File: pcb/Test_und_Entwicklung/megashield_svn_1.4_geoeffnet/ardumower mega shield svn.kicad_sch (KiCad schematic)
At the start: 21 parts, among them K3 RELAY_2RT, P16 RPI Backup P., P17 RPI Main P., P42 Charger, P43 Battery, P49 MotorStop, Q1 BC847B

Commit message: megashield_svn_1.4_geoeffnet
megashield_svn_1.4_geoeffnet
29 BY1-BY12 JLCCPCB Nummer ergänzt
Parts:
- D10: Funktion Schalt-Diode, 75 V, 150 mA, SOD-123 -> (none); JLCPCB LCSC Part (none) -> C81598
- D77: JLCPCB LCSC Part (none) -> C81598
- EF1: JLCPCB Basic / Extern (none) -> 1; JLCPCB LCSC Part (none) -> C83797
- EF2: JLCPCB Basic / Extern (none) -> 1; JLCPCB LCSC Part (none) -> C312012
- EF3: JLCPCB Basic / Extern (none) -> 1; JLCPCB LCSC Part (none) -> C312004
- K3: Printfassung für Relais R: FIN 95.15.2 -> (none)
- Q1: JLCPCB Basic / Extern (none) -> 1; JLCPCB LCSC Part (none) -> C8575
- R10, R13: JLCPCB LCSC Part (none) -> C95519
- R12, R9: JLCPCB LCSC Part (none) -> C95527
- R18: JLCPCB LCSC Part (none) -> C4190
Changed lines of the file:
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@@
       (effects (font (size 1.27 1.27)) hide)
     )
-    (property "JLCPCB LCSC Part" "" (id 6) (at 111.76 62.484 0)
+    (property "JLCPCB LCSC Part" "C95527" (id 6) (at 111.76 62.484 0)
       (effects (font (size 1.27 1.27)) hide)
     )
@@
       (effects (font (size 1.27 1.27)) hide)
     )
-    (property "JLCPCB LCSC Part" "" (id 6) (at 111.76 78.232 0)
+    (property "JLCPCB LCSC Part" "C95519" (id 6) (at 111.76 78.232 0)
       (effects (font (size 1.27 1.27)) hide)
     )
@@
       (effects (font (size 1.27 1.27)) hide)
     )
-    (property "JLCPCB LCSC Part" "" (id 6) (at 133.858 99.568 0)
+    (property "JLCPCB LCSC Part" "C4190" (id 6) (at 133.858 99.568 0)
       (effects (font (size 1.27 1.27)) hide)
     )
@@
       (effects (font (size 1.27 1.27)) hide)
     )
-    (property "JLCPCB LCSC Part" "" (id 6) (at 212.725 69.469 0)
+    (property "JLCPCB LCSC Part" "C95527" (id 6) (at 212.725 69.469 0)
       (effects (font (size 1.27 1.27)) hide)
     )
@@
       (effects (font (size 1.27 1.27)) hide)
     )
-    (property "JLCPCB LCSC Part" "" (id 6) (at 212.725 85.217 0)
+    (property "JLCPCB LCSC Part" "C95519" (id 6) (at 212.725 85.217 0)
       (effects (font (size 1.27 1.27)) hide)
     )
@@
       (effects (font (size 1.27 1.27)) hide)
     )
+    (property "JLCPCB Basic / Extern" "1" (id 6) (at 52.197 51.816 0)
+      (effects (font (size 1.27 1.27)) hide)
+    )
+    (property "JLCPCB LCSC Part" "C83797" (id 7) (at 52.197 51.816 0)
+      (effects (font (size 1.27 1.27)) hide)
+    )
   )
   (symbol (lib_id "ardumower-mega-shield-svn-rescue:F_10A-RESCUE-ardumower_mega_shield_svn") (at 186.69 52.959 270) (unit 1)
@@
       (effects (font (size 1.27 1.27)) hide)
     )
+    (property "JLCPCB Basic / Extern" "1" (id 6) (at 186.69 52.959 0)
+      (effects (font (size 1.27 1.27)) hide)
+    )
+    (property "JLCPCB LCSC Part" "C312012" (id 7) (at 186.69 52.959 0)
+      (effects (font (size 1.27 1.27)) hide)
+    )
   )
   (symbol (lib_id "ardumower-mega-shield-svn-rescue:F_10A-RESCUE-ardumower_mega_shield_svn") (at 201.803 39.116 270) (unit 1)
@@
       (effects (font (size 1.27 1.27)) hide)
     )
+    (property "JLCPCB Basic / Extern" "1" (id 6) (at 201.803 39.116 0)
+      (effects (font (size 1.27 1.27)) hide)
+    )
+    (property "JLCPCB LCSC Part" "C312004" (id 7) (at 201.803 39.116 0)
+      (effects (font (size 1.27 1.27)) hide)
+    )
   )
   (symbol (lib_id "ardumower-mega-shield-svn-rescue:CP_Small-RESCUE-ardumower_mega_shield_svn") (at 120.269 84.455 0) (mirror y) (unit 1)
@@
       (effects (font (size 1.27 1.27)) hide)
     )
-    (property "Funktion" "Schalt-Diode, 75 V, 150 mA, SOD-123" (id 4) (at 144.272 78.359 0)
+    (property "JLCPCB LCSC Part" "C81598" (id 8) (at 144.272 78.359 0)
       (effects (font (size 1.27 1.27)) hide)
     )
-    (property "Gehäuseart" "SOD-123" (id 5) (at 144.272 78.359 0)
+    (property "Gehäuseart" "SOD-123" (id 4) (at 144.272 78.359 0)
       (effects (font (size 1.27 1.27)) hide)
     )
-    (property "Reichelt-Bestellnummer" "R: RND 1N4148W" (id 6) (at 144.272 78.359 0)
+    (property "Reichelt-Bestellnummer" "R: RND 1N4148W" (id 5) (at 144.272 78.359 0)
       (effects (font (size 1.27 1.27)) hide)
     )
-    (property "Bestücken (Assemble)" "JA (YES)" (id 7) (at 144.272 78.359 0)
+    (property "Bestücken (Assemble)" "JA (YES)" (id 6) (at 144.272 78.359 0)
       (effects (font (size 1.27 1.27)) hide)
     )
@@
       (effects (font (size 1.27 1.27)) hide)
     )
+    (property "JLCPCB LCSC Part" "C81598" (id 8) (at 198.374 64.262 0)
+      (effects (font (size 1.27 1.27)) hide)
+    )
   )
   (symbol (lib_id "ardumower-mega-shield-svn-rescue:D-RESCUE-ardumower_mega_shield_svn") (at 198.501 60.706 180) (unit 1)
@@
       (effects (font (size 1.27 1.27)) hide)
     )
+    (property "JLCPCB Basic / Extern" "1" (id 7) (at 148.082 99.568 0)
+      (effects (font (size 1.27 1.27)) hide)
+    )
+    (property "JLCPCB LCSC Part" "C8575" (id 8) (at 148.082 99.568 0)
+      (effects (font (size 1.27 1.27)) hide)
+    )
   )
   (symbol (lib_id "ardumower-mega-shield-svn-rescue:RELAY_2RT-RESCUE-ardumower_mega_shield_svn") (at 160.782 64.516 0) (unit 1)
@@
       (effects (font (size 1.524 1.524)) hide)
     )
-    (property "Printfassung für Relais" "R: FIN 95.15.2" (id 9) (at 160.782 64.516 0)
-      (effects (font (size 1.524 1.524)) hide)
-    )
-    (property "Bestücken (Assemble)" "NEIN (NO)" (id 4) (at 160.782 64.516 0)
+    (property "Bestelllink" "http://www.reichelt.de/Print-Steckrelais/FIN-40-52-9-6V/3/index.html?&ACTION=3&LA=2&ARTICLE=8108&GROUPID=3293&artnr=FIN+40.52.9+6V" (id 5) (at 160.782 64.516 0)
       (effects (font (size 1.27 1.27)) hide)
     )
-    (property "Bestelllink" "http://www.reichelt.de/Print-Steckrelais/FIN-40-52-9-6V/3/index.html?&ACTION=3&LA=2&ARTICLE=8108&GROUPID=3293&artnr=FIN+40.52.9+6V" (id 4) (at 160.782 64.516 0)
+    (property "Bestücken (Assemble)" "NEIN (NO)" (id 4) (at 160.782 64.516 0)
       (effects (font (size 1.27 1.27)) hide)
     )
@@
     )
     (path "/00000000-0000-0000-0000-000057e646ff/00000000-0000-0000-0000-000057e64bd0"
-      (reference "D7") (unit 1) (value "SMD ZF 15") (footprint "Diodes_SMD:MiniMELF_Standard")
+      (reference "D7") (unit 1) (value "MM1Z15") (footprint "Diode_SMD:D_SOD-123")
     )
     (path "/00000000-0000-0000-0000-000057e646ff/00000000-0000-0000-0000-000057e9a340"
@@
     )
     (path "/00000000-0000-0000-0000-000057dd8e0c/00000000-0000-0000-0000-000057dda0d5"
-      (reference "D2") (unit 1) (value "SMD ZF 15") (footprint "Diodes_SMD:MiniMELF_Standard")
+      (reference "D2") (unit 1) (value "MM1Z15") (footprint "Diode_SMD:D_SOD-123")
     )
     (path "/00000000-0000-0000-0000-000057dd8e0c/00000000-0000-0000-0000-000057e89203"

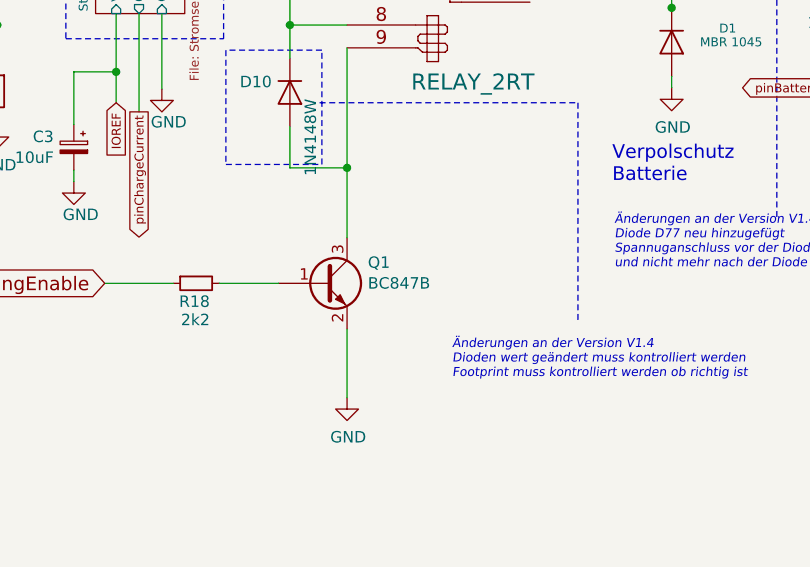
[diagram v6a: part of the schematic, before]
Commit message: megashield_svn_1.4_geoeffnet
megashield_svn_1.4_geoeffnet
32 Q3,Q12-Q23,Q1,Q38 neue JLCPCB Nummer
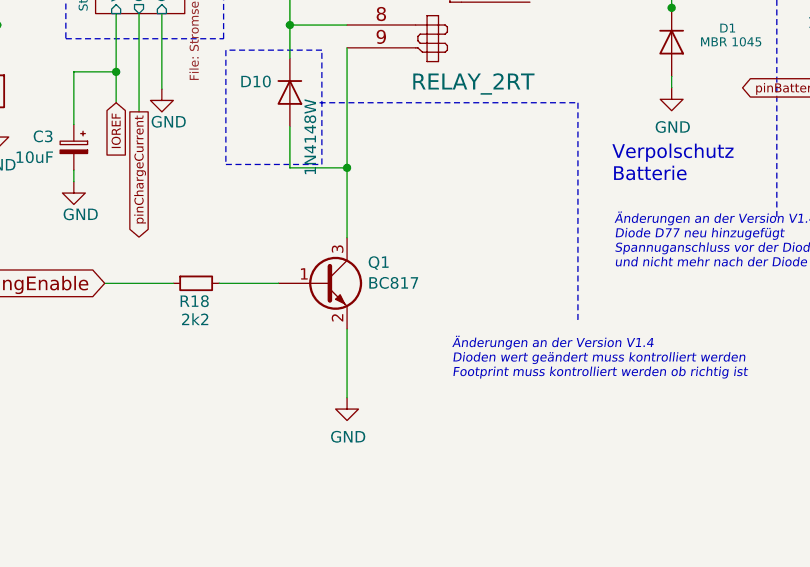
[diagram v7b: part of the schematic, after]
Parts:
- Q1: value BC847B -> BC817; Bestelllink https://www.reichelt.de/de/en/transistor-smd-npn-sot-23-45-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 -> https://www.reichelt.de/SB-SKE-4F-Dioden/S-1G-SMD/3/index.h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; Bestellnummer R: BC 847B SMD -> R: BC 817-40 SMD; Funktion Transistor SMD NPN SOT-23 45 V 0.1 A 0.25 W -> Transistor SMD NPN SOT-23 45 V 0.5 A 0.25 W; Gehäuseart SOT-23 -> SOT-23; JLCPCB LCSC Part C8575 -> C118725; Reichelt-Bestellnummer R: BC 847B SMD -> R: BC 817-40 SMD; Technische Daten Transistor SMD NPN SOT-23 45 V 0.1 A 0.25 W -> Transistor SMD NPN SOT-23 45 V 0.5 A 0.25 W
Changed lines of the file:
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@@
       (effects (font (size 1.27 1.27)) (justify left))
     )
-    (property "Value" "BC847B" (id 1) (at 152.9334 99.568 0)
+    (property "Value" "BC817" (id 1) (at 152.9334 99.568 0)
       (effects (font (size 1.27 1.27)) (justify left))
     )
@@
       (effects (font (size 1.27 1.27)) (justify left))
     )
-    (property "Gehäuseart" "SOT-23 " (id 4) (at 148.082 99.568 0)
+    (property "Gehäuseart" "SOT-23" (id 4) (at 148.082 99.568 0)
       (effects (font (size 1.524 1.524)) hide)
     )
-    (property "Bestelllink" "https://www.reichelt.de/de/en/transistor-smd-npn-sot-23-45-v-0-1-a-0-25-w-bc-847b-smd-p18562.html?GROUPID=7206&&r=1" (id 5) (at 148.082 99.568 0)
+    (property "Bestelllink" "https://www.reichelt.de/SB-SKE-4F-Dioden/S-1G-SMD/3/index.html?ACTION=3&LA=446&ARTICLE=95354&GROUPID=2991&artnr=S+1G+SMD&SEARCH=S%2B1G%2BSMD" (id 5) (at 148.082 99.568 0)
       (effects (font (size 1.524 1.524)) hide)
     )
-    (property "Technische Daten" "Transistor SMD NPN SOT-23 45 V 0.1 A 0.25 W" (id 6) (at 148.082 99.568 0)
+    (property "Technische Daten" "Transistor SMD NPN SOT-23 45 V 0.5 A 0.25 W" (id 6) (at 148.082 99.568 0)
       (effects (font (size 1.524 1.524)) hide)
     )
-    (property "Bestellnummer" "R: BC 847B SMD" (id 7) (at 148.082 99.568 0)
+    (property "Bestellnummer" "R: BC 817-40 SMD" (id 7) (at 148.082 99.568 0)
       (effects (font (size 1.524 1.524)) hide)
     )
@@
       (effects (font (size 1.27 1.27)) hide)
     )
-    (property "Funktion" "Transistor SMD NPN SOT-23 45 V 0.1 A 0.25 W" (id 5) (at 148.082 99.568 0)
+    (property "Funktion" "Transistor SMD NPN SOT-23 45 V 0.5 A 0.25 W" (id 5) (at 148.082 99.568 0)
       (effects (font (size 1.27 1.27)) hide)
     )
-    (property "Reichelt-Bestellnummer" "R: BC 847B SMD" (id 6) (at 148.082 99.568 0)
+    (property "Reichelt-Bestellnummer" "R: BC 817-40 SMD" (id 6) (at 148.082 99.568 0)
       (effects (font (size 1.27 1.27)) hide)
     )
@@
       (effects (font (size 1.27 1.27)) hide)
     )
-    (property "JLCPCB LCSC Part" "C8575" (id 8) (at 148.082 99.568 0)
+    (property "JLCPCB LCSC Part" "C118725" (id 8) (at 148.082 99.568 0)
       (effects (font (size 1.27 1.27)) hide)
     )
@@
     )
     (path "/00000000-0000-0000-0000-000057f1c5ee"
-      (reference "Q1") (unit 1) (value "BC847B") (footprint "TO_SOT_Packages_SMD:SOT-23")
+      (reference "Q1") (unit 1) (value "BC817") (footprint "TO_SOT_Packages_SMD:SOT-23")
     )
     (path "/00000000-0000-0000-0000-000058ab29d6"
@@
     )
     (path "/00000000-0000-0000-0000-000057dc7e7b/00000000-0000-0000-0000-000058e4d795"
-      (reference "Q38") (unit 1) (value "BC847B") (footprint "TO_SOT_Packages_SMD:SOT-23")
+      (reference "Q38") (unit 1) (value "BC817") (footprint "TO_SOT_Packages_SMD:SOT-23")
     )
     (path "/00000000-0000-0000-0000-000057dc7e7b/00000000-0000-0000-0000-000057dc8c57"
